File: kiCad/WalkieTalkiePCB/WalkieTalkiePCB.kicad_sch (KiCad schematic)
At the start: 23 parts, among them SW1 UP, SW2 DWN, SW3 MODE, SW4 TLK, SW5 XTRA, U1 I2S-INMP441_(MIC), U2 Amplifier, U3 ESP-WROOM-32, U4 I2S-128X64-OLED-LCD_, U5 PSM-301-Voltage-Regulator, U6 BAT-C-10TYPEC_(BMS), U7 PBS-LED-1606WH-L_(Toggle_Butt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

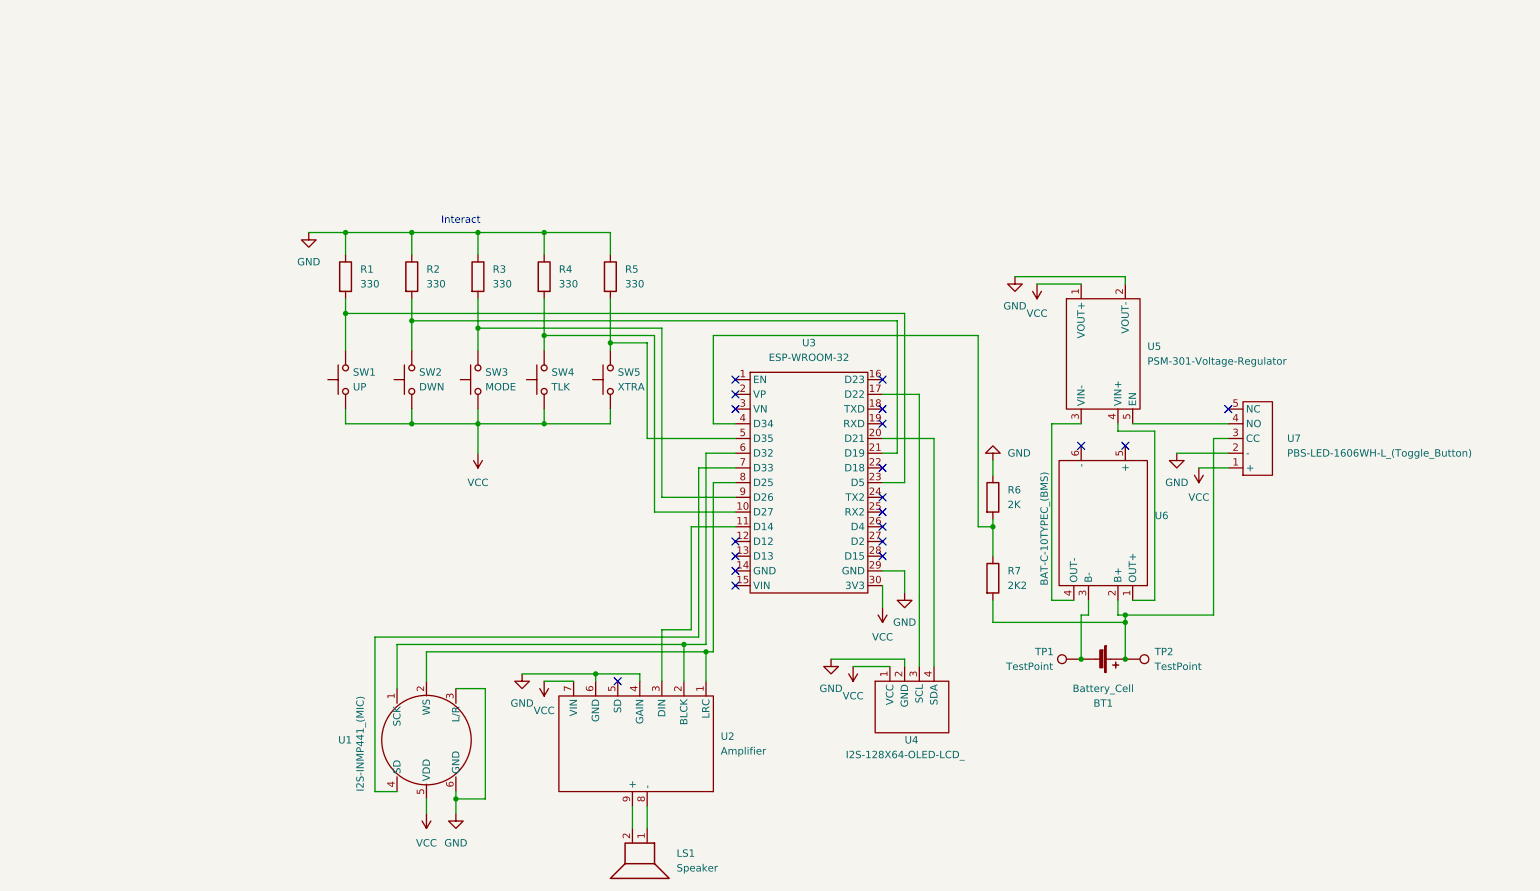
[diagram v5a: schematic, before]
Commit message: Updated Schematic Annotation
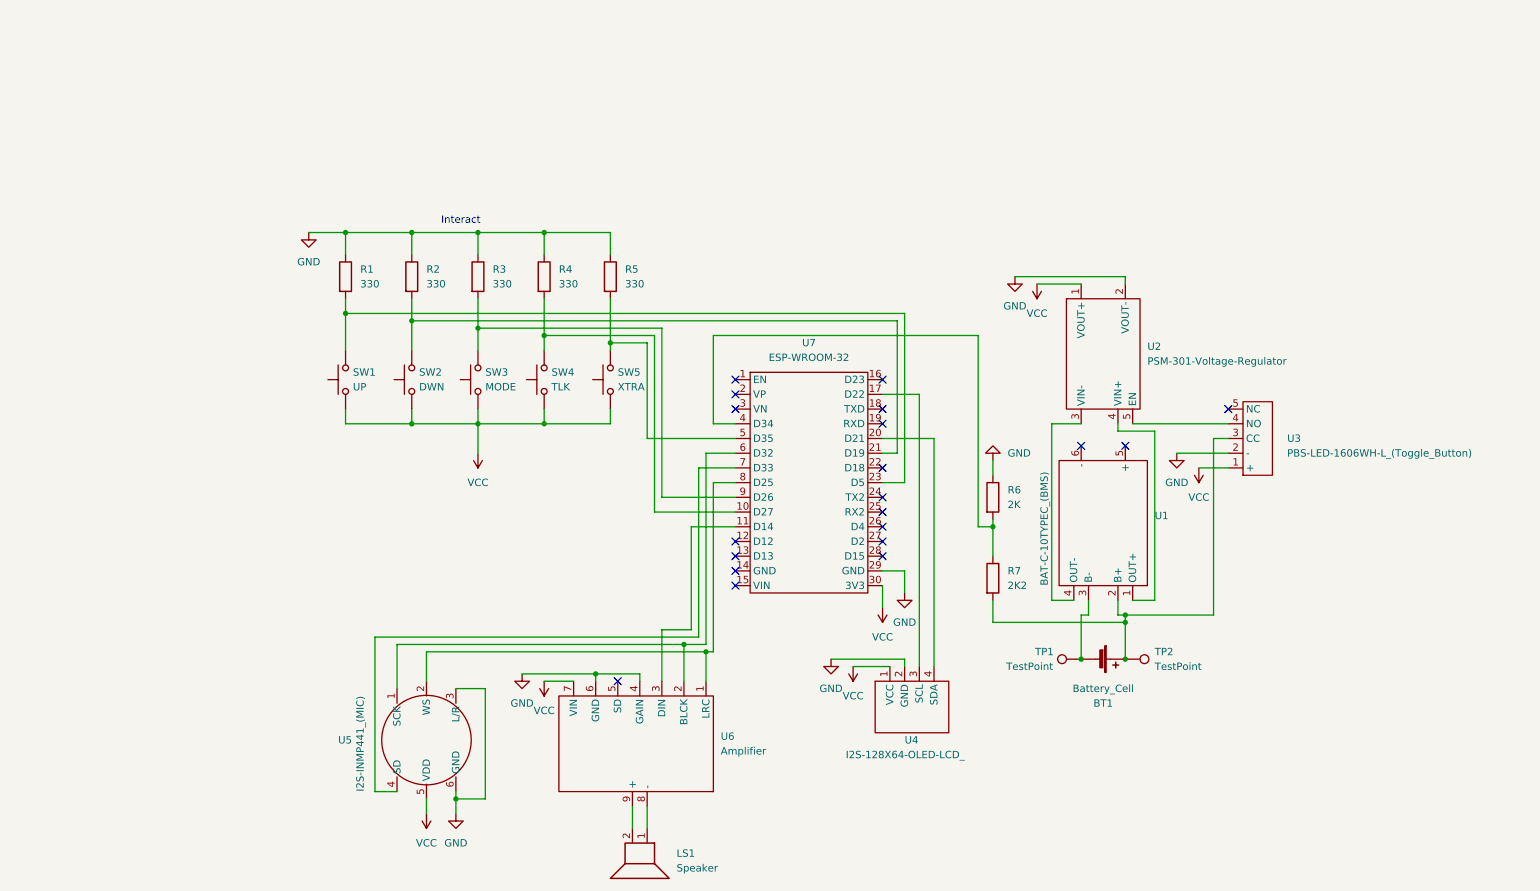
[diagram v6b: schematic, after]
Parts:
- renumbered U6 to U1, U5 to U2, U7 to U3, U1 to U5, U2 to U6, U3 to U7
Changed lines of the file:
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@@
   (symbol (lib_id "Walkie-Talkie-Symbols-Remastered:I2S-INMP441_(MIC)") (at 86.36 138.43 0) (unit 1)
     (in_bom yes) (on_board yes)
-    (property "Reference" "U1" (id 0) (at 71.12 138.43 0)
+    (property "Reference" "U5" (id 0) (at 71.12 138.43 0)
       (effects (font (size 1.27 1.27)) (justify left))
     )
@@
   (symbol (lib_id "Walkie-Talkie-Symbols-Remastered:PBS-LED-1606WH-L_(Toggle_Button)") (at 229.87 86.36 90) (unit 1)
     (in_bom yes) (on_board yes) (fields_autoplaced)
-    (property "Reference" "U7" (id 0) (at 234.95 86.3599 90)
+    (property "Reference" "U3" (id 0) (at 234.95 86.3599 90)
       (effects (font (size 1.27 1.27)) (justify right))
     )
@@
   (symbol (lib_id "Walkie-Talkie-Symbols-Remastered:BAT-C-10TYPEC_(BMS)") (at 203.2 97.79 180) (unit 1)
     (in_bom yes) (on_board yes)
-    (property "Reference" "U6" (id 0) (at 212.09 99.6949 0)
+    (property "Reference" "U1" (id 0) (at 212.09 99.6949 0)
       (effects (font (size 1.27 1.27)) (justify right))
     )
@@
   (symbol (lib_id "Walkie-Talkie-Symbols-Remastered:Amplifier") (at 123.19 140.97 180) (unit 1)
     (in_bom yes) (on_board yes) (fields_autoplaced)
-    (property "Reference" "U2" (id 0) (at 137.16 137.7949 0)
+    (property "Reference" "U6" (id 0) (at 137.16 137.7949 0)
       (effects (font (size 1.27 1.27)) (justify right))
     )
@@
   (symbol (lib_id "Walkie-Talkie-Symbols-Remastered:ESP-WROOM-32") (at 152.4 88.9 0) (unit 1)
     (in_bom yes) (on_board yes) (fields_autoplaced)
-    (property "Reference" "U3" (id 0) (at 152.4 69.85 0))
+    (property "Reference" "U7" (id 0) (at 152.4 69.85 0))
     (property "Value" "ESP-WROOM-32" (id 1) (at 152.4 72.39 0))
     (property "Footprint" "esp32_devkit_v1_doit:esp32_devkit_v1_doit" (id 2) (at 149.86 88.9 0)
@@
   (symbol (lib_id "Walkie-Talkie-Symbols-Remastered:PSM-301-Voltage-Regulator") (at 203.2 72.39 0) (unit 1)
     (in_bom yes) (on_board yes) (fields_autoplaced)
-    (property "Reference" "U5" (id 0) (at 210.82 70.4849 0)
+    (property "Reference" "U2" (id 0) (at 210.82 70.4849 0)
       (effects (font (size 1.27 1.27)) (justify left))
     )
@@
       (reference "TP2") (unit 1) (value "TestPoint") (footprint "")
     )
-    (path "/24e5f562-b3c9-438d-aa7d-32525f265570"
-      (reference "U1") (unit 1) (value "I2S-INMP441_(MIC)") (footprint "ESP32-Walkie-Talkie-Footprints-Remaster:I2SINMP441-MIC")
-    )
-    (path "/d187716d-bf1f-4766-8eed-da05cbe1a24f"
-      (reference "U2") (unit 1) (value "Amplifier") (footprint "ESP32-Walkie-Talkie-Footprints-Remaster:Amplifier")
-    )
-    (path "/db0f0dc4-d53d-49af-97d4-c1a1631d7dec"
-      (reference "U3") (unit 1) (value "ESP-WROOM-32") (footprint "esp32_devkit_v1_doit:esp32_devkit_v1_doit")
+    (path "/9a969628-52ab-4714-ac6a-9ca3d7003ab5"
+      (reference "U1") (unit 1) (value "BAT-C-10TYPEC_(BMS)") (footprint "ESP32-Walkie-Talkie-Footprints-Remaster:BAT-C-10TYPEC-BMS")
+    )
+    (path "/f9fa421f-31c6-4a6d-8614-790ab077f912"
+      (reference "U2") (unit 1) (value "PSM-301-Voltage-Regulator") (footprint "ESP32-Walkie-Talkie-Footprints-Remaster:PSM-301-Voltage-Regulator")
+    )
+    (path "/8d95fbde-1cc6-44c9-b9f6-c11098d1fc3f"
+      (reference "U3") (unit 1) (value "PBS-LED-1606WH-L_(Toggle_Button)") (footprint "ESP32-Walkie-Talkie-Footprints-Remaster:PBS-LED-1606WH-L-Toggle-Switch")
     )
     (path "/f8a305e8-0bc6-4f0a-b0fa-387fb8c70c45"
       (reference "U4") (unit 1) (value "I2S-128X64-OLED-LCD_") (footprint "ESP32-Walkie-Talkie-Footprints-Remaster:I2S-128x64-OLED-LCD")
     )
-    (path "/f9fa421f-31c6-4a6d-8614-790ab077f912"
-      (reference "U5") (unit 1) (value "PSM-301-Voltage-Regulator") (footprint "ESP32-Walkie-Talkie-Footprints-Remaster:PSM-301-Voltage-Regulator")
-    )
-    (path "/9a969628-52ab-4714-ac6a-9ca3d7003ab5"
-      (reference "U6") (unit 1) (value "BAT-C-10TYPEC_(BMS)") (footprint "ESP32-Walkie-Talkie-Footprints-Remaster:BAT-C-10TYPEC-BMS")
-    )
-    (path "/8d95fbde-1cc6-44c9-b9f6-c11098d1fc3f"
-      (reference "U7") (unit 1) (value "PBS-LED-1606WH-L_(Toggle_Button)") (footprint "ESP32-Walkie-Talkie-Footprints-Remaster:PBS-LED-1606WH-L-Toggle-Switch")
-    )
-  )
+    (path "/24e5f562-b3c9-438d-aa7d-32525f265570"
+      (reference "U5") (unit 1) (value "I2S-INMP441_(MIC)") (footprint "ESP32-Walkie-Talkie-Footprints-Remaster:I2SINMP441-MIC")
+    )
+    (path "/d187716d-bf1f-4766-8eed-da05cbe1a24f"
+      (reference "U6") (unit 1) (value "Amplifier") (footprint "ESP32-Walkie-Talkie-Footprints-Remaster:Amplifier")
+    )
+    (path "/db0f0dc4-d53d-49af-97d4-c1a1631d7dec"
+      (reference "U7") (unit 1) (value "ESP-WROOM-32") (footprint "esp32_devkit_v1_doit:esp32_devkit_v1_doit")
+    )
+  )
